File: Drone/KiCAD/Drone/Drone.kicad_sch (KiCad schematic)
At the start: 41 parts, among them M1 Motor_DC, M2 Motor_DC, M3 Motor_DC, M4 Motor_DC, SW1 SW_Push, U1 nRF24L01P, U2 LPS22DF, U3 STM32G431C8Tx, Y1 16MHz 12pF, Y2 16MHz 12pF

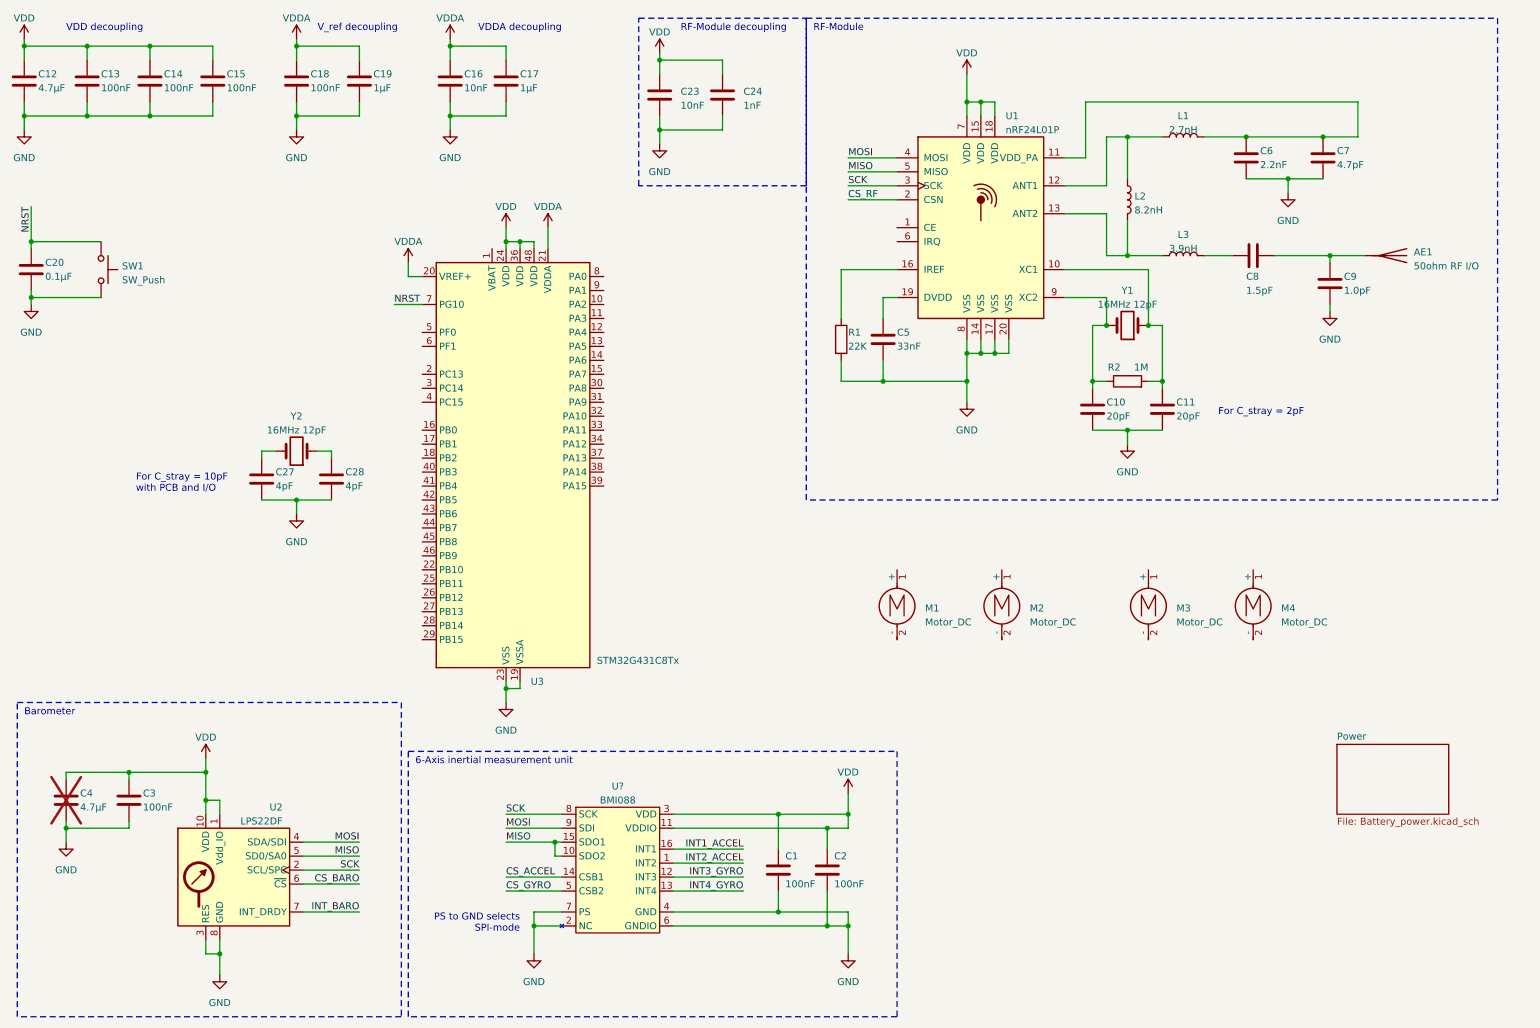
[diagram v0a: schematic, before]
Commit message: Added sheet formalities
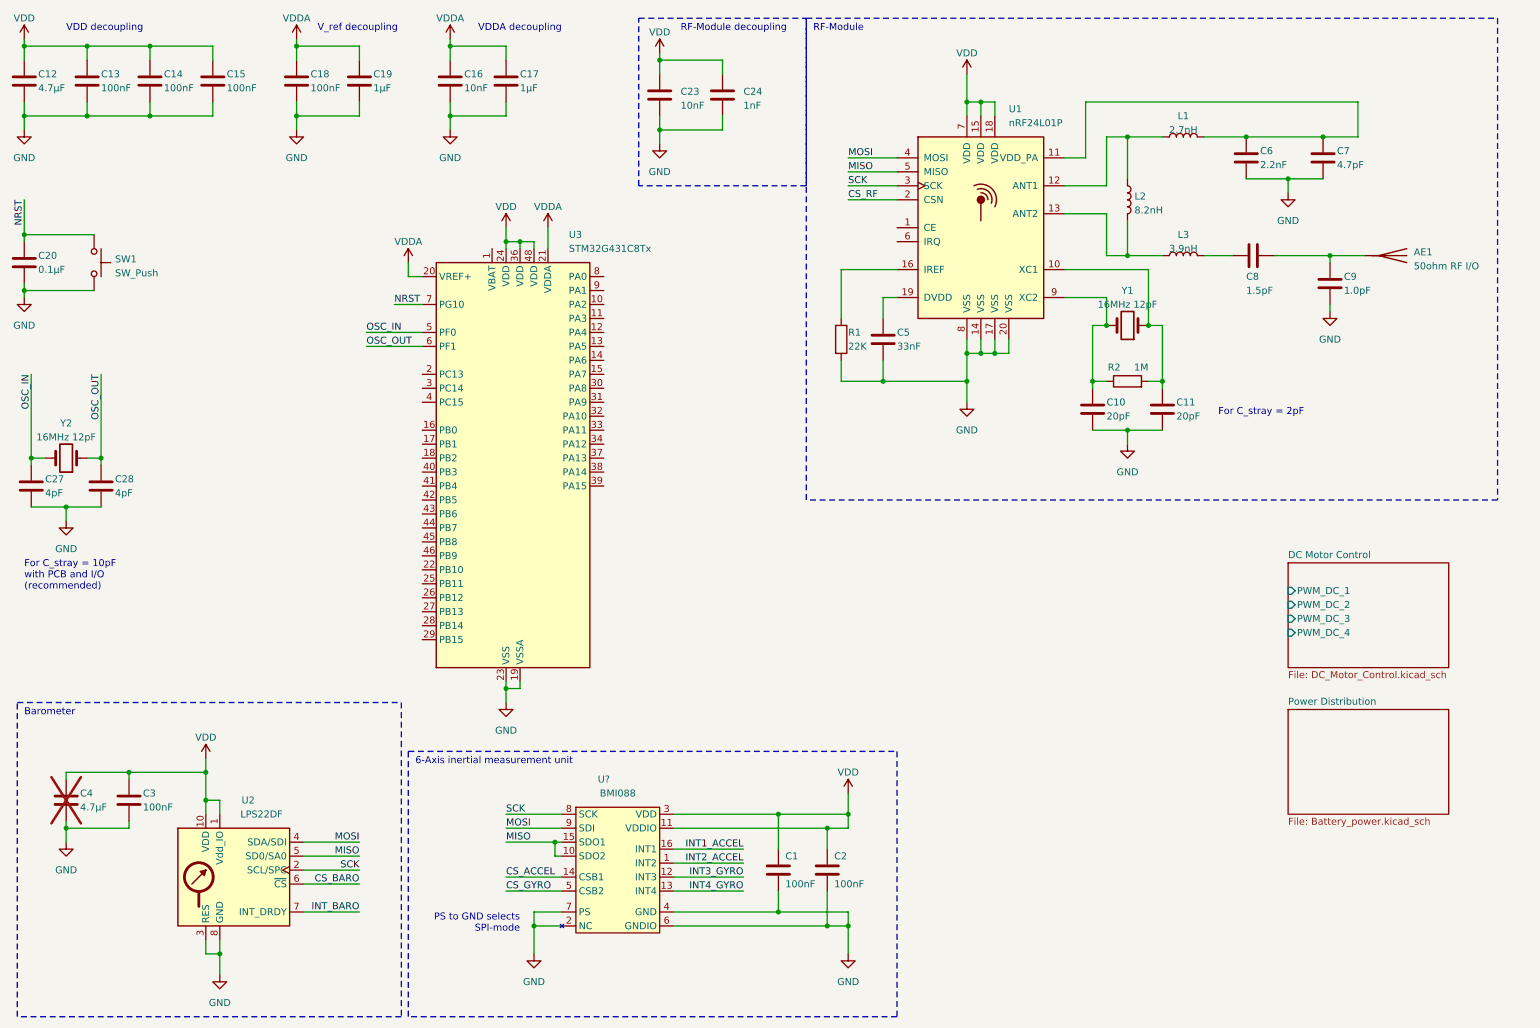
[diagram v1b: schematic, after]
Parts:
- removed M1, M2, M3, M4: Motor_DC, symbol Motor:Motor_DC
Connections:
- net OSC_OUT: now reaches C28.1, Y2.1
- net OSC_OUT: now also U3.6 (PF1)
- net OSC_IN: now reaches C27.1, Y2.2
- net OSC_IN: now also U3.5 (PF0)
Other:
- sheet Power renamed Power Distribution
- added sheet DC Motor Control (DC_Motor_Control.kicad_sch)
- note added: "For C_stray = 10pF with PCB and I/O (recommended)"
- note removed: "For C_stray = 10pF with PCB and I/O"
- title: (none) -> Lightweight Drone - Main Schematic
- moved on the sheet: C20, C27, C28, SW1, Y2

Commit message: Add files via upload
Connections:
- net CS_ACCEL is gone; now on net SPI_CS_ACCEL: U?.14 (CSB1)
- net CS_BARO is gone; now on net SPI_CS_BARO: U2.6 (~{CS})
- net CS_GYRO is gone; now on net SPI_CS_GYRO: U?.5 (CSB2)
- net CS_RF is gone; now on net SPI_CS_RF: U1.2 (CSN)
- net MISO is gone; now on net SPI_MISO: U1.5 (MISO), U2.5 (SD0/SA0), U?.10 (SDO2), U?.15 (SDO1)
- net MOSI is gone; now on net SPI_MOSI: U1.4 (MOSI), U2.4 (SDA/SDI), U?.9 (SDI)
- net SCK is gone; now on net SPI_SCK: U1.3 (SCK), U2.2 (SCL/SPC), U?.8 (SCK)
- net SPI_CS_GYRO: now reaches U3.10 (PA2)
- net SPI_CS_BARO: now reaches U3.11 (PA3)
- net TIM1_CH1: now reaches U3.30 (PA8)
- net TIM1_CH2: now reaches U3.31 (PA9)
- net TIM1_CH3: now reaches U3.32 (PA10)
- net TIM1_CH4: now reaches U3.33 (PA11)
- net SPI_SCK: now reaches U3.40 (PB3)
- net SPI_MISO: now reaches U3.41 (PB4)
- net SPI_MOSI: now reaches U3.42 (PB5)
- net BOOT0: now reaches U3.45 (PB8)
- net SPI_CS_RF: now reaches U3.8 (PA0)
- net SPI_CS_ACCEL: now reaches U3.9 (PA1)

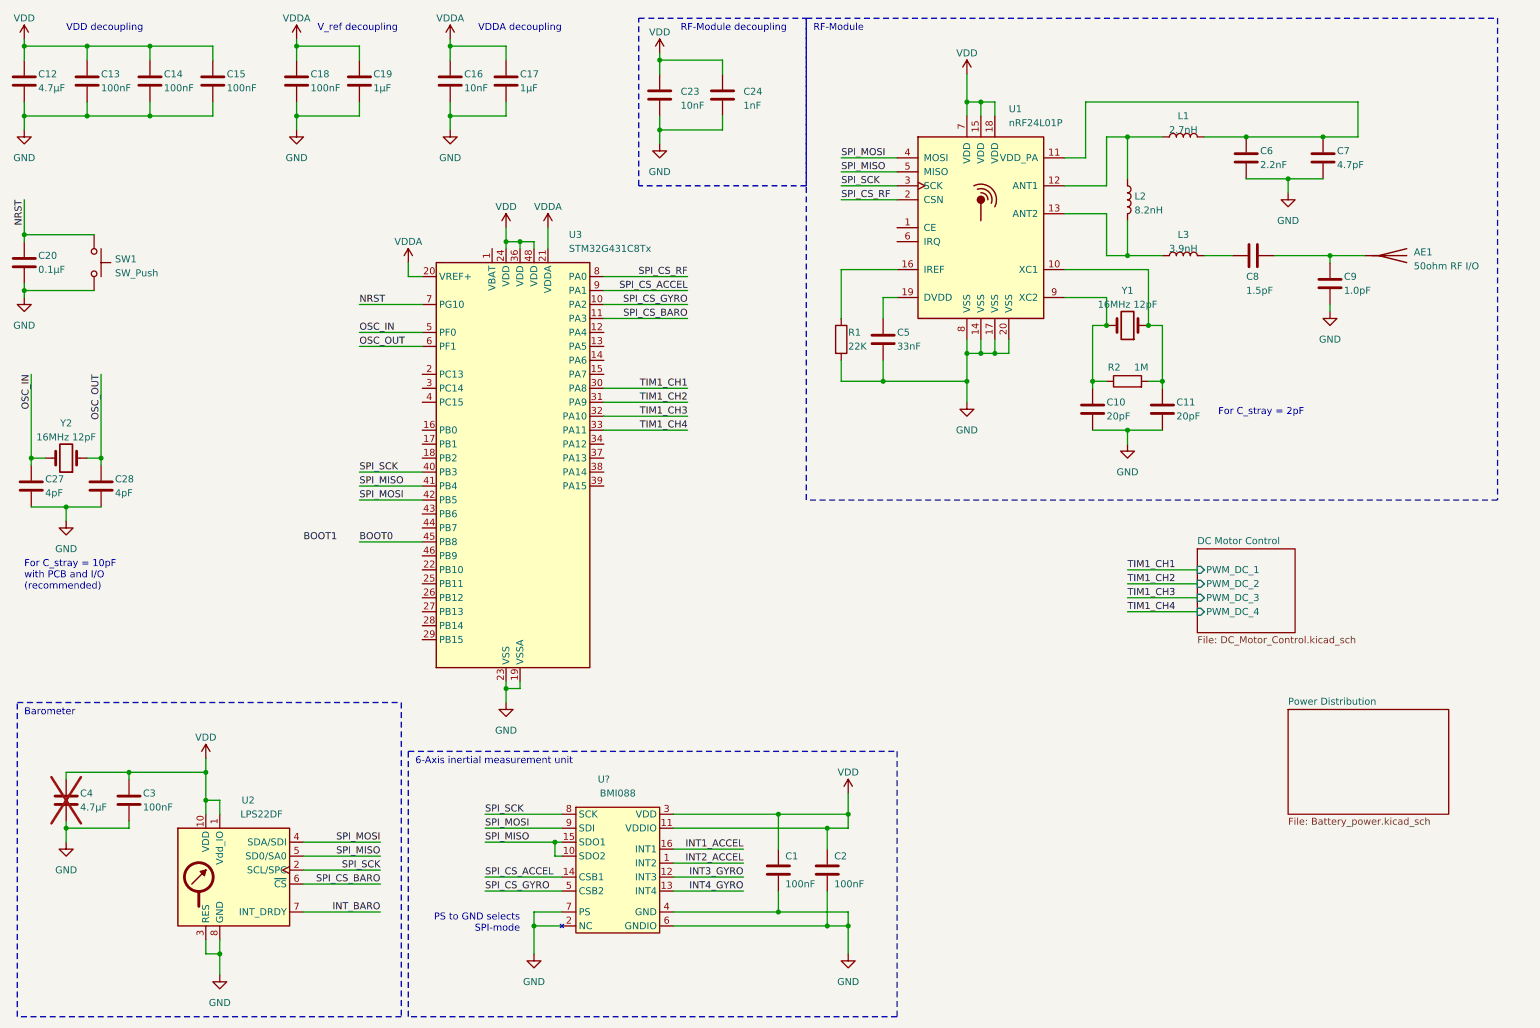
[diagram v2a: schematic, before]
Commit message: new LDO, programming and µC connections
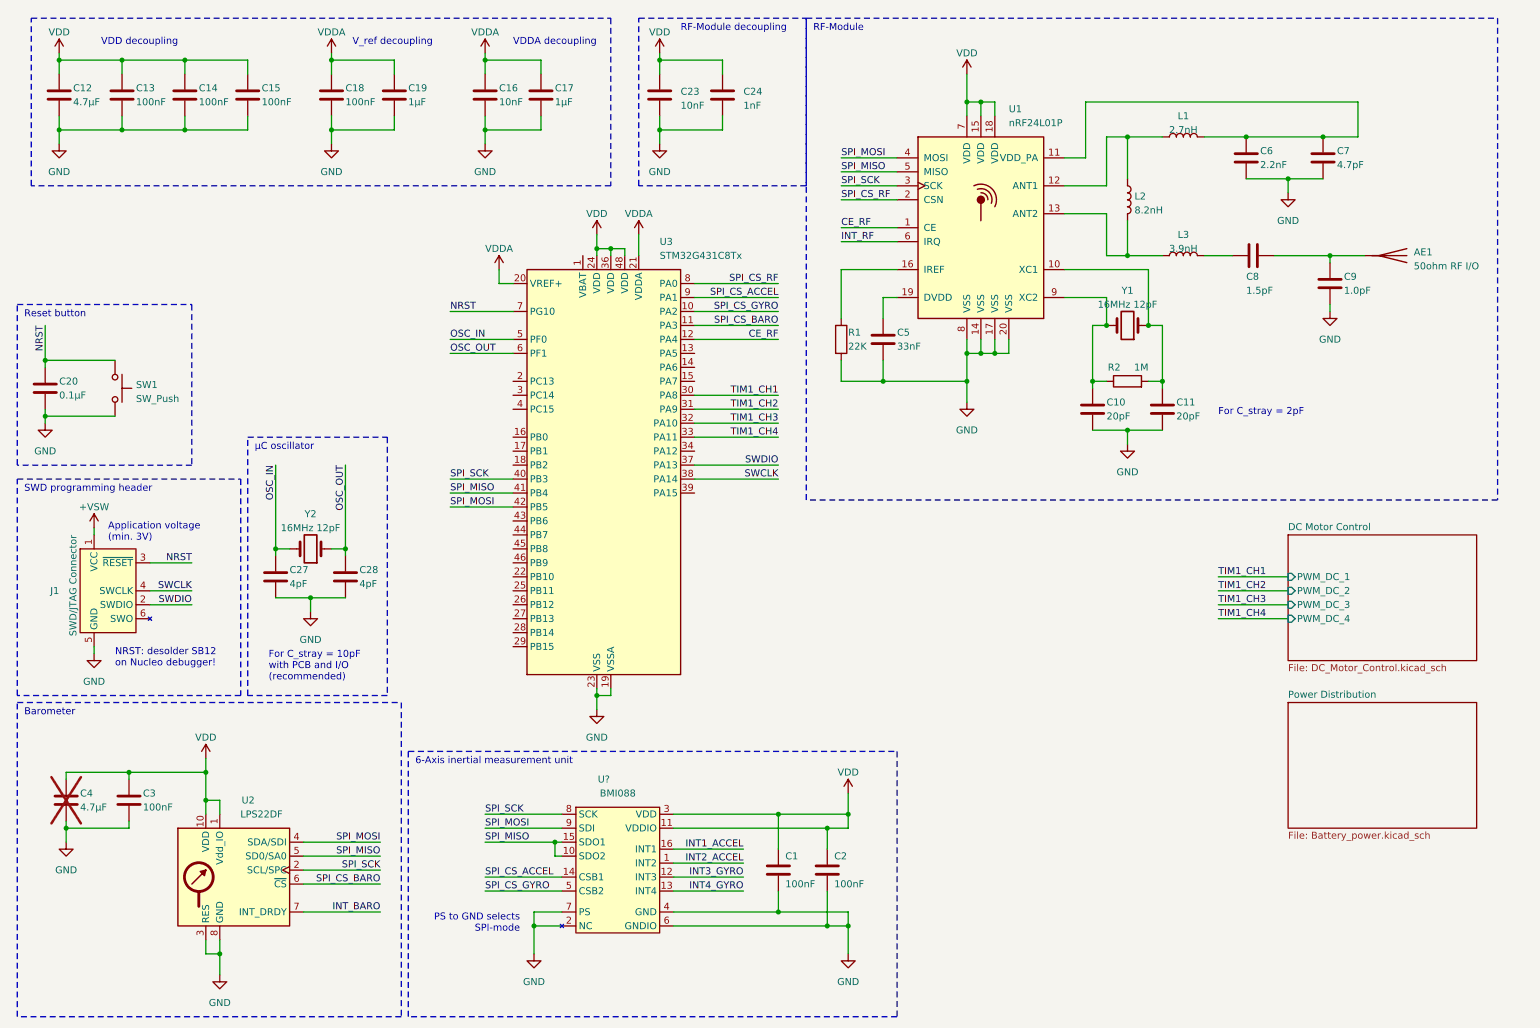
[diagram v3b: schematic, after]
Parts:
- added J1: SWD/JTAG Connector, Connector:Tag-Connect_TC2030-IDC-FP_2x03_P1.27mm_Vertical, symbol Connector:Conn_ARM_SWD_TagConnect_TC2030
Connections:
- net GND: now also J1.5 (GND)
- net NRST: now also J1.3 (~{RESET})
- net CE_RF: now reaches U3.12 (PA4)
- net CE_RF: now also U1.1 (CE)
- net SWDIO: now reaches U3.37 (PA13)
- net SWDIO: now also J1.2 (SWDIO)
- net SWCLK: now reaches U3.38 (PA14)
- net SWCLK: now also J1.4 (SWCLK)
- net INT_RF: now reaches U1.6 (IRQ)
- net BOOT0: no longer names the net of U3.45 (PB8)
- new net +VSW: J1.1 (VCC)
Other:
- note added: "Application voltage (min. 3V)"
- note added: "NRST: desolder SB12 on Nucleo debugger!"
- note added: "Reset button"
- note added: "SWD programming header"
- note added: "µC oscillator"
- moved on the sheet: C12, C13, C14, C15, C16, C17, C18, C19, C20, C27, C28, SW1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
